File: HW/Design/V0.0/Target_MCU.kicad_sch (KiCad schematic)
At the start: 36 parts, among them J3 EXP PORT, J5 QWIIC, Q6 SI2302, Q7 SI2302, U10 20MHz, U4 PIC16F877A

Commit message: PIC16-DevKit-PCB-877 PCB V0.0
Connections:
- net INT0: now also MD1.22 (D7); no longer MD1.21 (D6)
- net INT1: now also MD1.21 (D6); no longer MD1.22 (D7)
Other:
- company: (none) -> SAMPI DEVELOPMENT KITS
- title: (none) -> PIC16F877A DEV KIT
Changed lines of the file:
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@@
 	(generator_version "8.0")
 	(paper "A4")
+	(title_block
+		(title "PIC16F877A DEV KIT")
+		(date "2025-01-01")
+		(rev "0.0")
+		(company "SAMPI DEVELOPMENT KITS")
+		(comment 1 "P/N: SAMM-16F877A")
+	)
 	(junction
 		(at 60.96 124.46)
@@
 	(hierarchical_label "INT0"
 		(shape output)
-		(at 194.31 130.81 0)
+		(at 194.31 128.27 0)
 		(fields_autoplaced yes)
 		(effects
@@
 	(hierarchical_label "INT1"
 		(shape output)
-		(at 194.31 128.27 0)
-		(fields_autoplaced yes)
-		(effects
+		(at 194.31 130.81 0)
+		(fields_autoplaced yes)
+		(effects

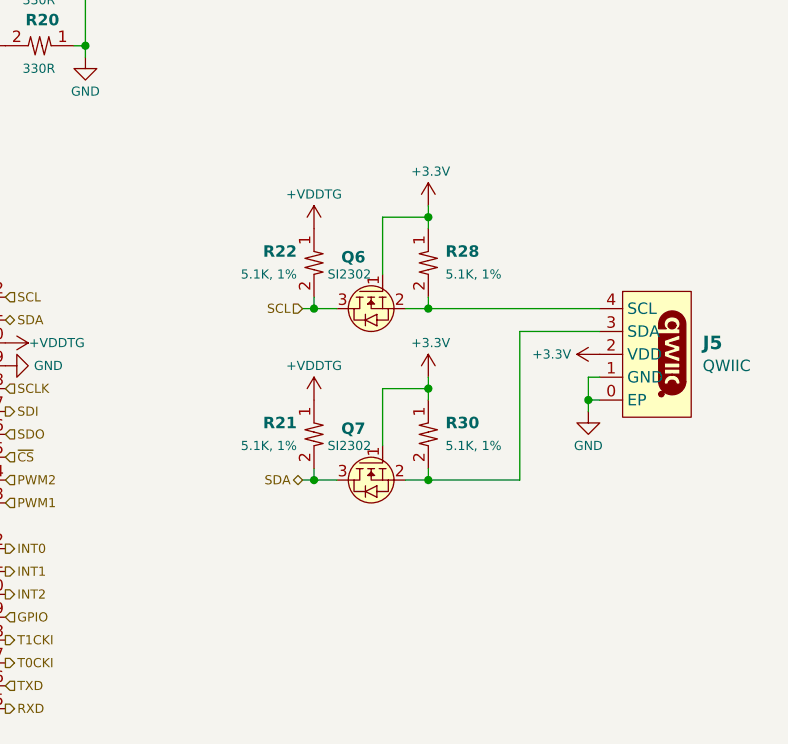
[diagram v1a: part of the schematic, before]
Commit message: PIC16-DevKit-PCB-877 V0.1 - QWIIC ESD protection, disable VPP, detect VBUS, measure VPP, VDDTG
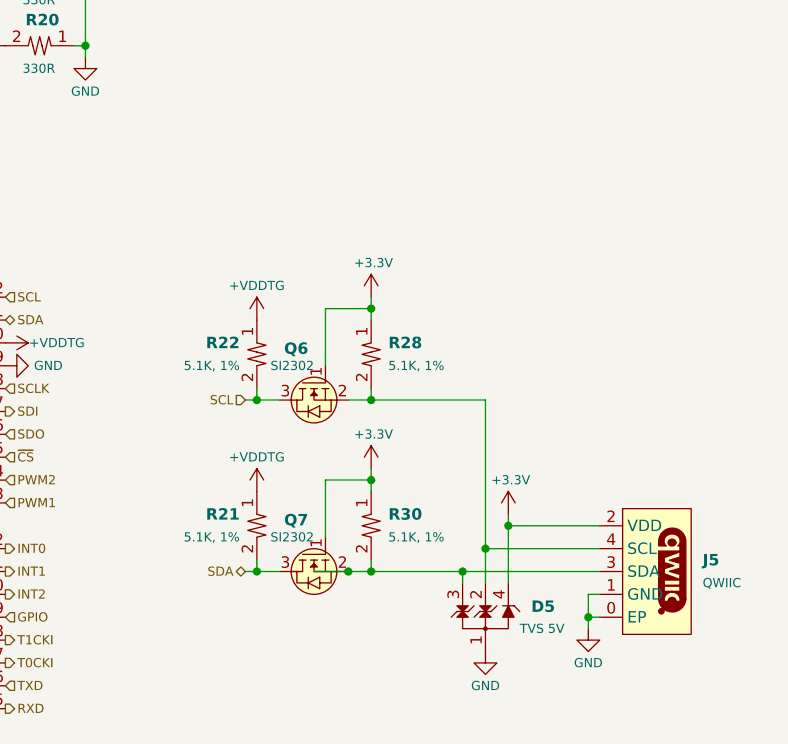
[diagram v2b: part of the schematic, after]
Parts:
- added D5: TVS 5V, SAMPI:SOT143B_NEXT, symbol SAMPI:TVS_3CH
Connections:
- net +3.3V: now also D5.4 (CH3)
- net GND: now also D5.1 (GND)
- net at J5.4 (SCL), Q6.2 (S), R28.2: now also D5.2 (CH1)
- net at J5.3 (SDA), Q7.2 (S), R30.2: now also D5.3 (CH2)
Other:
- moved on the sheet: J5, Q6, Q7, R21, R22, R28, R30
